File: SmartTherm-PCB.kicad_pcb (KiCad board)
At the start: 2 copper layers, 85.1 x 35.6 mm, 22 parts, among them J1 Junkers, J2 Display - Sensor, J3 Ext LDR, Q1 BC546, U1 WeMos D1 mini, U2 ILD74, U3 LM358

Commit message: update BOM
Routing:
- net +3V3: track 79.7 -> 82.7 mm
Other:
- board text added: "SmartTherm V3.0"
- board text removed: "SmartTherm V2.0"
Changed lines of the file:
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@@
 			(remove_unused_layers no)
 			(net 10 "GND")
+			(thermal_bridge_angle 0)
 		)
 	)
@@
 			(remove_unused_layers no)
 			(net 10 "GND")
+			(thermal_bridge_angle 0)
 		)
 	)
@@
 			(remove_unused_layers no)
 			(net 10 "GND")
+			(thermal_bridge_angle 0)
 		)
 	)
@@
 			(remove_unused_layers no)
 			(net 10 "GND")
+			(thermal_bridge_angle 0)
 		)
 	)
@@
 		)
 	)
-	(gr_text "SmartTherm V2.0"
+	(gr_text "SmartTherm V3.0"
 		(at 128.778 102.108 0)
 		(layer "F.SilkS")
@@
 	)
 	(segment
+		(start 172.72 105.41)
+		(end 178.99 105.41)
+		(width 1)
+		(layer "F.Cu")
+		(net 1)
+	)
+	(segment
+		(start 154.94 86.36)
+		(end 159.385 81.915)
+		(width 1)
+		(layer "F.Cu")
+		(net 1)
+	)
+	(segment
+		(start 183.515 100.885)
+		(end 180.34 104.06)
+		(width 1)
+		(layer "F.Cu")
+		(net 1)
+	)
+	(segment
+		(start 160.655 102.87)
+		(end 163.195 102.87)
+		(width 1)
+		(layer "F.Cu")
+		(net 1)
+	)
+	(segment
+		(start 175.055 84.25)
+		(end 179.5 84.25)
+		(width 1)
+		(layer "F.Cu")
+		(net 1)
+	)
+	(segment
 		(start 183.515 88.265)
 		(end 183.515 100.885)
@@
 	)
 	(segment
-		(start 172.72 105.41)
-		(end 178.99 105.41)
+		(start 172.72 81.915)
+		(end 175.055 84.25)
+		(width 1)
+		(layer "F.Cu")
+		(net 1)
+	)
+	(segment
+		(start 152.4 86.36)
+		(end 154.94 86.36)
 		(width 1)
 		(layer "F.Cu")
@@
 	)
 	(segment
-		(start 160.655 102.87)
-		(end 163.195 102.87)
-		(width 1)
-		(layer "F.Cu")
-		(net 1)
-	)
-	(segment
-		(start 152.4 86.36)
-		(end 154.94 86.36)
-		(width 1)
-		(layer "F.Cu")
-		(net 1)
-	)
-	(segment
-		(start 172.72 81.915)
-		(end 174.625 83.82)
-		(width 1)
-		(layer "F.Cu")
-		(net 1)
-	)
-	(segment
-		(start 154.94 86.36)
-		(end 159.385 81.915)
-		(width 1)
-		(layer "F.Cu")
-		(net 1)
-	)
-	(segment
-		(start 179.07 83.82)
-		(end 183.515 88.265)
-		(width 1)
-		(layer "F.Cu")
-		(net 1)
-	)
-	(segment
 		(start 163.195 102.87)
 		(end 165.735 105.41)
@@
 	)
 	(segment
+		(start 179.5 84.25)
+		(end 183.515 88.265)
+		(width 1)
+		(layer "F.Cu")
+		(net 1)
+	)
+	(segment
 		(start 165.735 105.41)
 		(end 172.72 105.41)
@@
 	)
 	(segment
-		(start 174.625 83.82)
-		(end 179.07 83.82)
-		(width 1)
-		(layer "F.Cu")
-		(net 1)
-	)
-	(segment
-		(start 183.515 100.885)
-		(end 180.34 104.06)
-		(width 1)
-		(layer "F.Cu")
-		(net 1)
-	)
-	(segment
 		(start 165.1 98.425)
 		(end 160.655 102.87)
@@
 	)
 	(segment
+		(start 131.85 81.293679)
+		(end 133.363679 79.78)
+		(width 1)
+		(layer "F.Cu")
+		(net 5)
+	)
+	(segment
 		(start 123.19 86.36)
-		(end 134.62 74.93)
+		(end 131.85 86.36)
 		(width 1)
 		(layer "F.Cu")
@@
 	)
 	(segment
-		(start 171.05 78.74)
+		(start 138.97 79.78)
+		(end 143.82 74.93)
+		(width 1)
+		(layer "F.Cu")
+		(net 5)
+	)
+	(segment
+		(start 133.363679 79.78)
+		(end 138.97 79.78)
+		(width 1)
+		(layer "F.Cu")
+		(net 5)
+	)
+	(segment
+		(start 143.82 74.93)
 		(end 167.005 74.93)
 		(width 1)
@@
 	)
 	(segment
-		(start 134.62 74.93)
-		(end 135.255 74.93)
+		(start 131.85 86.36)
+		(end 131.85 81.293679)
 		(width 1)
 		(layer "F.Cu")
@@
 	(segment
 		(start 167.005 74.93)
-		(end 135.255 74.93)
+		(end 171.05 78.74)
 		(width 1)
 		(layer "F.Cu")
@@
 	)
 	(segment
-		(start 172.72 73.66)
-		(end 180.34 81.28)
-		(width 0.5)
-		(layer "F.Cu")
-		(net 23)
-	)
-	(segment
 		(start 123.19 81.915)
 		(end 121.285 83.82)
@@
 	)
 	(segment
-		(start 131.445 73.66)
-		(end 123.19 81.915)
+		(start 143.09 73.66)
+		(end 137.92 78.83)
 		(width 0.5)
 		(layer "F.Cu")
@@
 	)
 	(segment
-		(start 131.445 73.66)
+		(start 172.72 73.66)
+		(end 143.09 73.66)
+		(width 0.5)
+		(layer "F.Cu")
+		(net 23)
+	)
+	(segment
+		(start 132.42 78.83)
+		(end 129.335 81.915)
+		(width 0.5)
+		(layer "F.Cu")
+		(net 23)
+	)
+	(segment
+		(start 180.34 81.28)
 		(end 172.72 73.66)
+		(width 0.5)
+		(layer "F.Cu")
+		(net 23)
+	)
+	(segment
+		(start 137.92 78.83)
+		(end 132.42 78.83)
 		(width 0.5)
 		(layer "F.Cu")
@@
 		(start 121.285 83.82)
 		(end 116.84 83.82)
+		(width 0.5)
+		(layer "F.Cu")
+		(net 23)
+	)
+	(segment
+		(start 129.335 81.915)
+		(end 123.19 81.915)
 		(width 0.5)
 		(layer "F.Cu")
@@
 		(polygon
 			(pts
-				(xy 140.97 80.01) (xy 115.57 80.01) (xy 115.57 73.025) (xy 140.97 73.025)
-			)
-		)
+				(xy 140.97 80.01) (xy 115.57 80.01) (xy 115.57 72.275) (xy 140.97 72.275)
+			)
+		)

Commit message: updates to pass ERC/DRC
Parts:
- R1, R10, R3, R4, R5, R6, R7, R8, R9: footprint Resistor_THT:R_Axial_DIN0207_L6.3mm_D2.5mm_P10.16mm_Horizontal -> 1projectLibrary:R_Axial_DIN0207_L6.3mm_D2.5mm_P10.16mm_Horizontal
- U1: footprint Module:WEMOS_D1_mini_light -> 1projectLibrary:WEMOS_D1_mini_light
- moved J3 0.84 mm to (179.5, 81.2)
- moved J1 0.84 mm to (179.5, 104.1)
- moved R6 0.29 mm to (167.6, 97.5)
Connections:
- net +3V3 renamed +3.3V
- net /24Present renamed /24V-Present
- U1 pad 1: Net-(U1-Pad1) -> unconnected-(U1-~{RST}-Pad1)
- U1 pad 11: Net-(U1-Pad11) -> unconnected-(U1-D4-Pad11)
- U1 pad 13: Net-(U1-Pad13) -> unconnected-(U1-SDA/D2-Pad13)
- U1 pad 3: Net-(U1-Pad3) -> unconnected-(U1-D0-Pad3)
- U1 pad 4: Net-(U1-Pad4) -> unconnected-(U1-SCK/D5-Pad4)
- U1 pad 5: Net-(U1-Pad5) -> unconnected-(U1-MISO/D6-Pad5)
- U1 pad 6: Net-(U1-Pad6) -> unconnected-(U1-MOSI/D7-Pad6)
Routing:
- net GND: track 216.6 -> 49.0 mm
- net Net-(J1-Pin_2): track 15.2 -> 14.4 mm
- net +3.3V: track 82.7 -> 81.9 mm

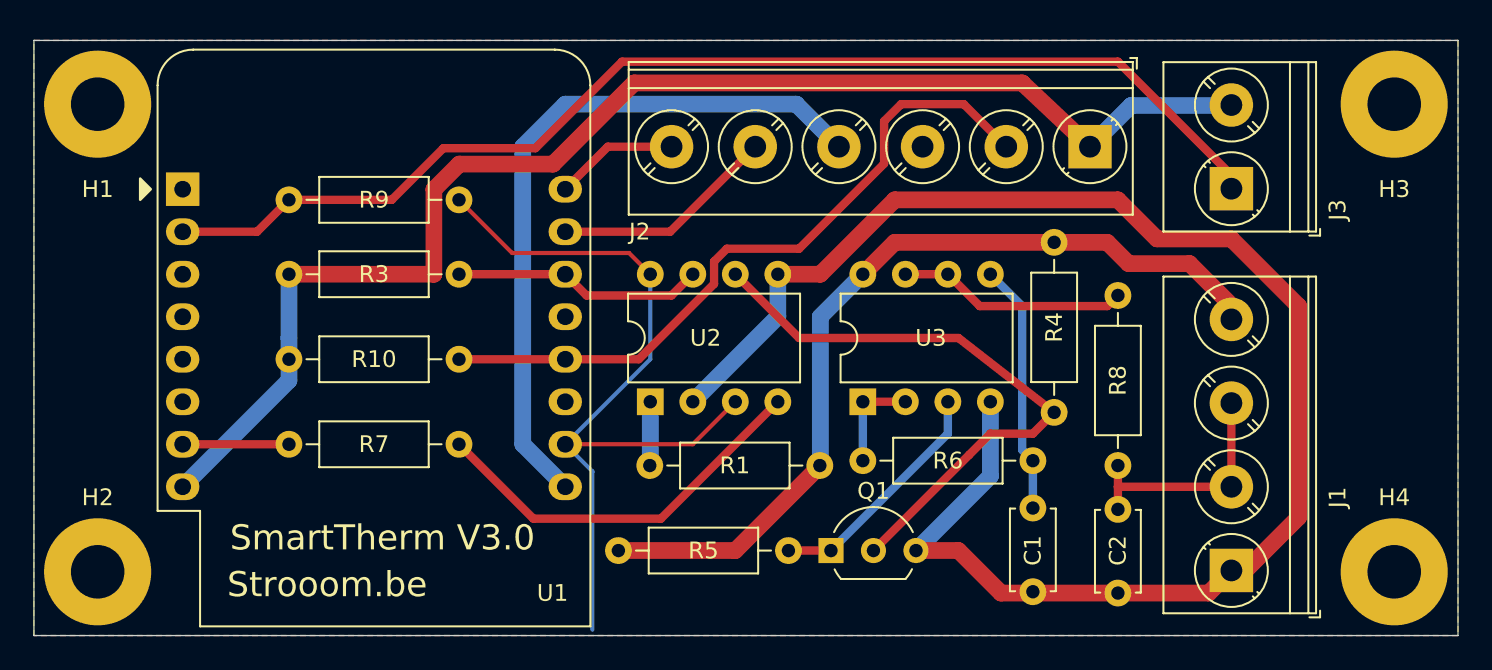
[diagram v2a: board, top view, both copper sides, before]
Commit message: footprint updates
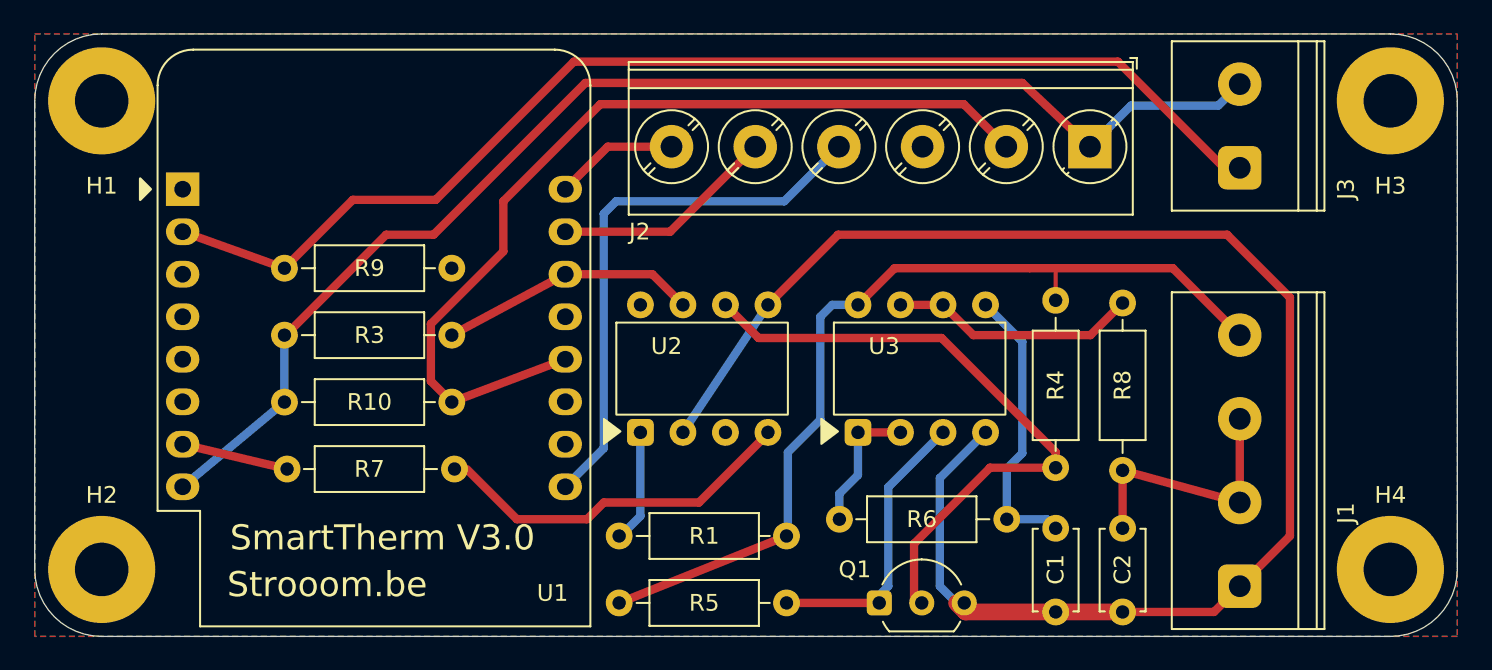
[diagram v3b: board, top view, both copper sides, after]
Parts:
- C1, C2: footprint Capacitor_THT:C_Disc_D4.7mm_W2.5mm_P5.00mm -> 1projectLibrary:C_Disc_D4.7mm_W2.5mm_P5.00mm
- J1: footprint TerminalBlock_Phoenix:TerminalBlock_Phoenix_PT-1,5-4-5.0-H_1x04_P5.00mm_Horizontal -> 1projectLibrary:TerminalBlock_Junkers
- J3: footprint TerminalBlock_Phoenix:TerminalBlock_Phoenix_PT-1,5-2-5.0-H_1x02_P5.00mm_Horizontal -> 1projectLibrary:TerminalBlock_LDR
- Q1: footprint Package_TO_SOT_THT:TO-92L_Inline_Wide -> 1projectLibrary:TO-92L_Inline_Wide
- U2, U3: footprint Package_DIP:DIP-8_W7.62mm -> 1projectLibrary:DIP-8_W7.62mm
- moved R4 8.55 mm to (169.0, 93.0)
- moved R6 7.51 mm to (161.0, 101.0)
- moved R9 6.31 mm to (128.0, 86.0)
- moved Q1 6.26 mm to (161.0, 106.0)
- moved R3 6.03 mm to (128.0, 90.0)
- moved R5 6.01 mm to (148.0, 106.0)
- moved R7 5.55 mm to (128.0, 98.0)
- moved R10 5.45 mm to (128.0, 94.0)
- moved R1 5.32 mm to (148.0, 102.0)
- moved R8 4.80 mm to (173.0, 93.0)
- moved U3 4.04 mm to (161.0, 92.0), turned to 0 degrees
- moved C1 3.91 mm to (169.0, 104.0)
- moved U2 3.78 mm to (148.0, 92.0), turned to 0 degrees
- moved C2 3.60 mm to (173.0, 104.0)
- moved J3 1.35 mm to (180.0, 80.0)
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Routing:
- net GND: track 49.0 -> 0.53 mm
- net /Tin: track 42.3 -> 55.1 mm
- net +5V: track 42.4 -> 33.0 mm
- net +3.3V: track 81.9 -> 78.3 mm
- net Net-(Q1-C): track 14.3 -> 17.4 mm
- net Net-(R1-Pad1): track 3.82 -> 6.68 mm
- net +24V: track 51.9 -> 54.7 mm
- net GND2: track 94.4 -> 91.6 mm
- net Net-(R7-Pad1): track 24.1 -> 21.4 mm
- net Net-(U3B-+): track 15.0 -> 17.2 mm
- net Net-(U3A--): track 6.06 -> 8.19 mm
- net /Drive2: track 36.4 -> 38.2 mm
- net Net-(J1-Pin_2): track 14.4 -> 15.7 mm
- net Net-(U3B--): track 13.8 -> 14.8 mm
- net Net-(J3-Pin_1): track 70.5 -> 71.3 mm
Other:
- board size 85.1 x 35.6 mm -> 85 x 36 mm
